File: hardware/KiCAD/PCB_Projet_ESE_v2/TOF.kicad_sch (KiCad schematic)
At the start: 8 parts, among them J10 Conn_01x06, J11 Conn_01x06, J12 Conn_01x06, J13 Conn_01x06, J14 Conn_01x06, J15 Conn_01x06

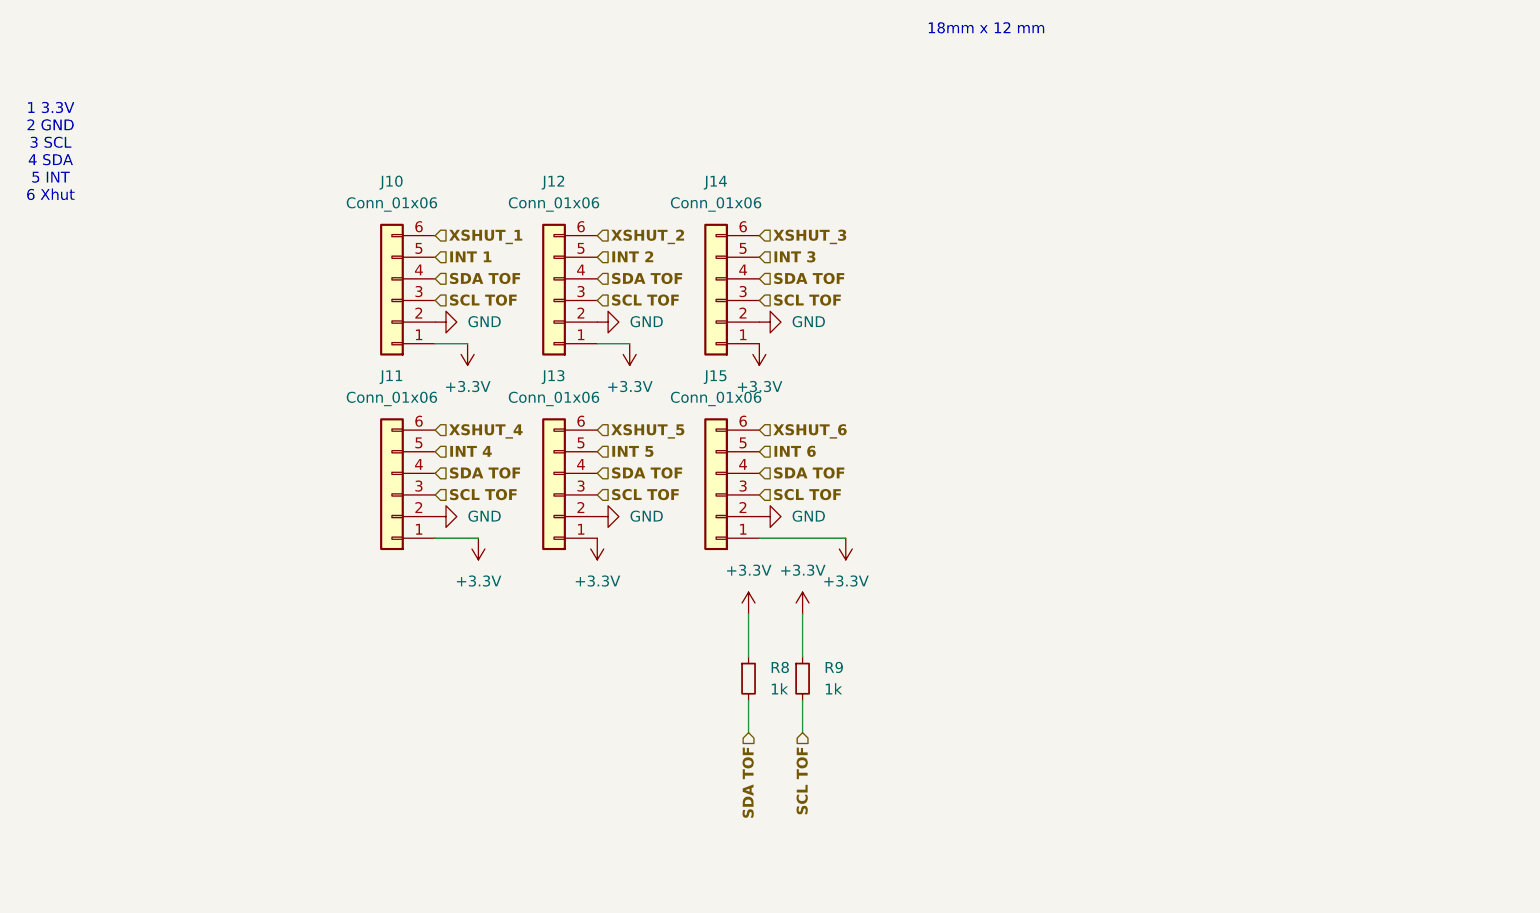
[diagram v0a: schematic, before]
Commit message: Schematic done for PCB v2
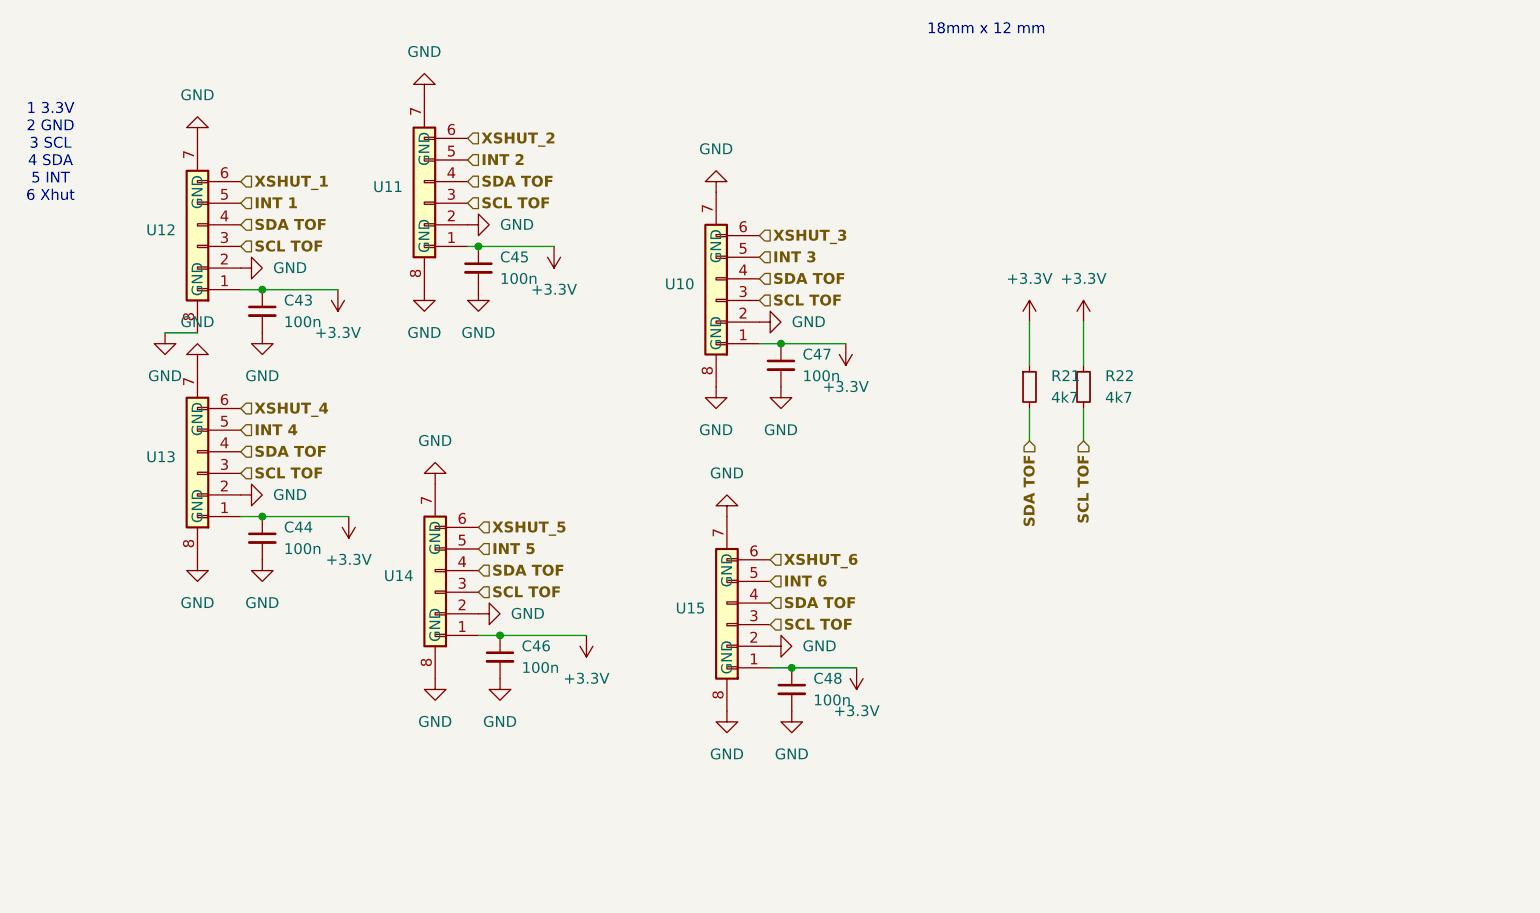
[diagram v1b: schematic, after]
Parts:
- removed J10, J11, J12, J13, J14, J15: Conn_01x06, mylib:JST_SH_6_Vertical, symbol Connector_Generic:Conn_01x06
- added C43, C44, C45, C46, C47, C48: 100n, Capacitor_SMD:C_0402_1005Metric, symbol Device:C_Small
- added U10, U11, U12, U13, U14, U15: ~, mylib:JST_SH_6_Vertical, symbol my_lib:JST_SH_6_Vertical
- R21: renamed from R8; value 1k -> 4k7
- R22: renamed from R9; value 1k -> 4k7
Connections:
- net +3.3V: now also C43.1, C44.1, C45.1, C46.1, C47.1, C48.1, U10.1, U11.1, U12.1, U13.1, U14.1, U15.1
- net GND: now also C43.2, C44.2, C45.2, C46.2, C47.2, C48.2, U10.2, U10.7 (GND), U10.8 (GND), U11.2, U11.7 (GND), U11.8 (GND), U12.2, U12.7 (GND), U12.8 (GND), U13.2, U13.7 (GND), U13.8 (GND), U14.2, U14.7 (GND), U14.8 (GND), U15.2, U15.7 (GND), U15.8 (GND)
- net INT 1: now also U12.5
- net INT 2: now also U11.5
- net INT 3: now also U10.5
- net INT 4: now also U13.5
- net INT 5: now also U14.5
- net INT 6: now also U15.5
- net SCL TOF: now also U10.3, U11.3, U12.3, U13.3, U14.3, U15.3
- net SDA TOF: now also U10.4, U11.4, U12.4, U13.4, U14.4, U15.4
- net XSHUT_1: now also U12.6
- net XSHUT_2: now also U11.6
- net XSHUT_3: now also U10.6
- net XSHUT_4: now also U13.6
- net XSHUT_5: now also U14.6
- net XSHUT_6: now also U15.6
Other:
- moved on the sheet: R21, R22

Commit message: PCB V2 routage v2 finished
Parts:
- added D1, D21, D22, D23, D24, D25: BLUE_LED_0402, LED_SMD:LED_0402_1005Metric, symbol Device:LED
- added R25, R26, R27, R28, R39, R40: 200, Resistor_SMD:R_0201_0603Metric, symbol Device:R_Small
- U10, U11, U12, U13, U14, U15: footprint mylib:JST_SH_6_Vertical -> mylib:Wurth_Vertical_6_pos_0.8mm
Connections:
- net +3.3V: now also R25.2, R26.2, R27.2, R28.2, R39.2, R40.2
- net INT 1: now also D1.1 (K)
- net INT 2: now also D21.1 (K)
- net INT 3: now also D22.1 (K)
- net INT 4: now also D25.1 (K)
- net INT 5: now also D24.1 (K)
- net INT 6: now also D23.1 (K)
- new net: D25.2 (A), R40.1
- new net: D23.2 (A), R28.1
- new net: D24.2 (A), R39.1
- new net: D22.2 (A), R27.1
- new net: D1.2 (A), R25.1
- new net: D21.2 (A), R26.1
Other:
- note added: "150040BS73240"
- note added: "TNPW0201200RBEED"
